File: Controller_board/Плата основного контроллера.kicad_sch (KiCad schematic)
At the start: 38 parts, among them J3 DebugUSART (PinHeader_01x03_P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, J4 Debug GPIO (PinHeader_01x02_P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, Q1 DTC114ECA (SOT-23), Q2 DTC114ECA (SOT-23), U1 ADM3485EARZ-REEL (SOIC-8), U2 ADUM1401CRWZ-RL, SO16W, U5 SMU02N-05

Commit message: Change ISOLATOR 03.06.24
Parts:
- removed U2: ADUM1401CRWZ-RL, SO16W, Package_SO:SOIC-16W_7.5x10.3mm_P1.27mm, symbol Isolator:ADuM1401xRW
- added U2: π141M3x, Package_SO:SOIC-16_3.9x9.9mm_P1.27mm, symbol Isolator:π141M3x
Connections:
- net +3.3VRS485: now also U2.16 (VDD2)
- net +5V: now also U2.1 (VDD1)
- net GND1: now also U2.15 (GND2), U2.9 (GND2)
- net GNDD: now also U2.2 (GND1), U2.8 (GND1)
- net USART2_RTS: now also U2.5 (VIC)
- net USART2_RX: now also U2.6 (VOD)
- net USART2_TX: now also U2.4 (VIB)
- net at R1.1, U1.1 (RO): now also U2.11 (VID)
- net at R2.1: now also U2.10 (VE2)
- net at R7.2, U1.2 (~{RE}), U1.3 (DE): now also U2.12 (VOC)
- net at U1.4 (DI): now also U2.13 (VOB)
- net at R5.2: now also U2.7 (VE1)
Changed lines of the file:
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@@
-    )
-  )
-  (symbol (lib_id "Isolator:ADuM1401xRW") (at 138.43 43.18 180) (unit 1)
-    (in_bom yes) (on_board yes) (dnp no)
-    (property "Reference" "U2" (at 138.43 25.4 0)
-      (effects (font (size 1.27 1.27)))
-    )
-    (property "Value" "ADUM1401CRWZ-RL, SO16W" (at 138.43 27.94 0)
-      (effects (font (size 1.27 1.27)))
-    )
-    (property "Footprint" "Package_SO:SOIC-16W_7.5x10.3mm_P1.27mm" (at 138.43 28.575 0)
-      (effects (font (size 1.27 1.27)) hide)
-    )
-    (property "Datasheet" "https://www.analog.com/media/en/technical-documentation/data-sheets/ADUM1400_1401_1402.pdf" (at 158.75 43.18 0)
-      (effects (font (size 1.27 1.27)) hide)
-    )
-    (pin "10")
-    (pin "9")
-    (pin "4")
-    (pin "8")
-    (pin "1")
-    (pin "13")
-    (pin "2")
-    (pin "11")
-    (pin "7")
-    (pin "5")
-    (pin "12")
-    (pin "3")
-    (pin "6")
-    (pin "14")
-    (pin "16")
-    (pin "15")
-    (instances
-      (project "Плата основного контроллера"
-        (path "/0ad4c27f-47f6-4faf-ae8a-ed32884f7b20"
-          (reference "U2") (unit 1)
-        )
-      )
-      (project "Плата внешних шаговых двигателей"
-        (path "/7f8f7dc9-8c50-44ed-985c-35a6d8c67be0/0d239b34-7914-40bc-9b83-7e562c30defe"
-          (reference "U4") (unit 1)
-        )
-        (path "/7f8f7dc9-8c50-44ed-985c-35a6d8c67be0"
-          (reference "U2") (unit 1)
-        )
-      )
     )
   )
@@
         )
       )
+    )
+  )
+  (symbol (lib_id "Isolator:π141M3x") (at 138.43 43.18 180) (unit 1)
+    (in_bom yes) (on_board yes) (dnp no) (fields_autoplaced)
+    (property "Reference" "U2" (at 138.43 25.4 0)
+      (effects (font (size 1.27 1.27)))
+    )
+    (property "Value" "π141M3x" (at 138.43 27.94 0)
+      (effects (font (size 1.27 1.27)))
+    )
+    (property "Footprint" "Package_SO:SOIC-16_3.9x9.9mm_P1.27mm" (at 138.43 28.575 0)
+      (effects (font (size 1.27 1.27)) hide)
+    )
+    (property "Datasheet" "https://wmsc.lcsc.com/wmsc/upload/file/pdf/v2/lcsc/2001082007_2Pai-Semi--141M30_C471604.pdf" (at 158.75 43.18 0)
+      (effects (font (size 1.27 1.27)) hide)
+    )
+    (pin "6")
+    (pin "16")
+    (pin "11")
+    (pin "13")
+    (pin "10")
+    (pin "12")
+    (pin "3")
+    (pin "14")
+    (pin "4")
+    (pin "8")
+    (pin "5")
+    (pin "2")
+    (pin "9")
+    (pin "7")
+    (pin "15")
+    (pin "1")
+    (instances
+      (project "Плата основного контроллера"
+        (path "/0ad4c27f-47f6-4faf-ae8a-ed32884f7b20"
+          (reference "U2") (unit 1)
+        )
+      )

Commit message: pcb and schems main controller 07.06.24
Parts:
- added TP1 (x9): TestPoint, PCM_4ms_TestPoint:TestPoint_D1, symbol Connector:TestPoint
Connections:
- net +5V: now also TP1.1
- net GND1: now also RS1.5 (Pin_5), RS1.6 (Pin_6), RS3.7 (Pin_7), RS3.8 (Pin_8)
- net UART6_DE: now also J3.1 (Pin_1); no longer J3.3 (Pin_3)
- net USART2_RTS: now also TP1.1
- net USART2_RX: now also TP1.1
- net USART2_TX: now also TP1.1
- net USART6_RX: now also J3.3 (Pin_3); no longer J3.2 (Pin_2)
- net USART6_TX: now also J3.2 (Pin_2); no longer J3.1 (Pin_1)
- net at R31.1, R6.2, RS1.4 (Pin_4)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: now also TP1.1
- net at R3.1, R31.2, RS1.3 (Pin_3)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: now also TP1.1
- net at R1.1, U1.1 (RO), U2.11 (VID): now also TP1.1
- net at R7.2, U1.2 (~{RE}), U1.3 (DE)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: now also TP1.1
- net at U1.4 (DI), U2.13 (VOB): now also TP1.1
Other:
- sheet RTS_ISO ports: added +3.3V; removed none
- moved on the sheet: R5

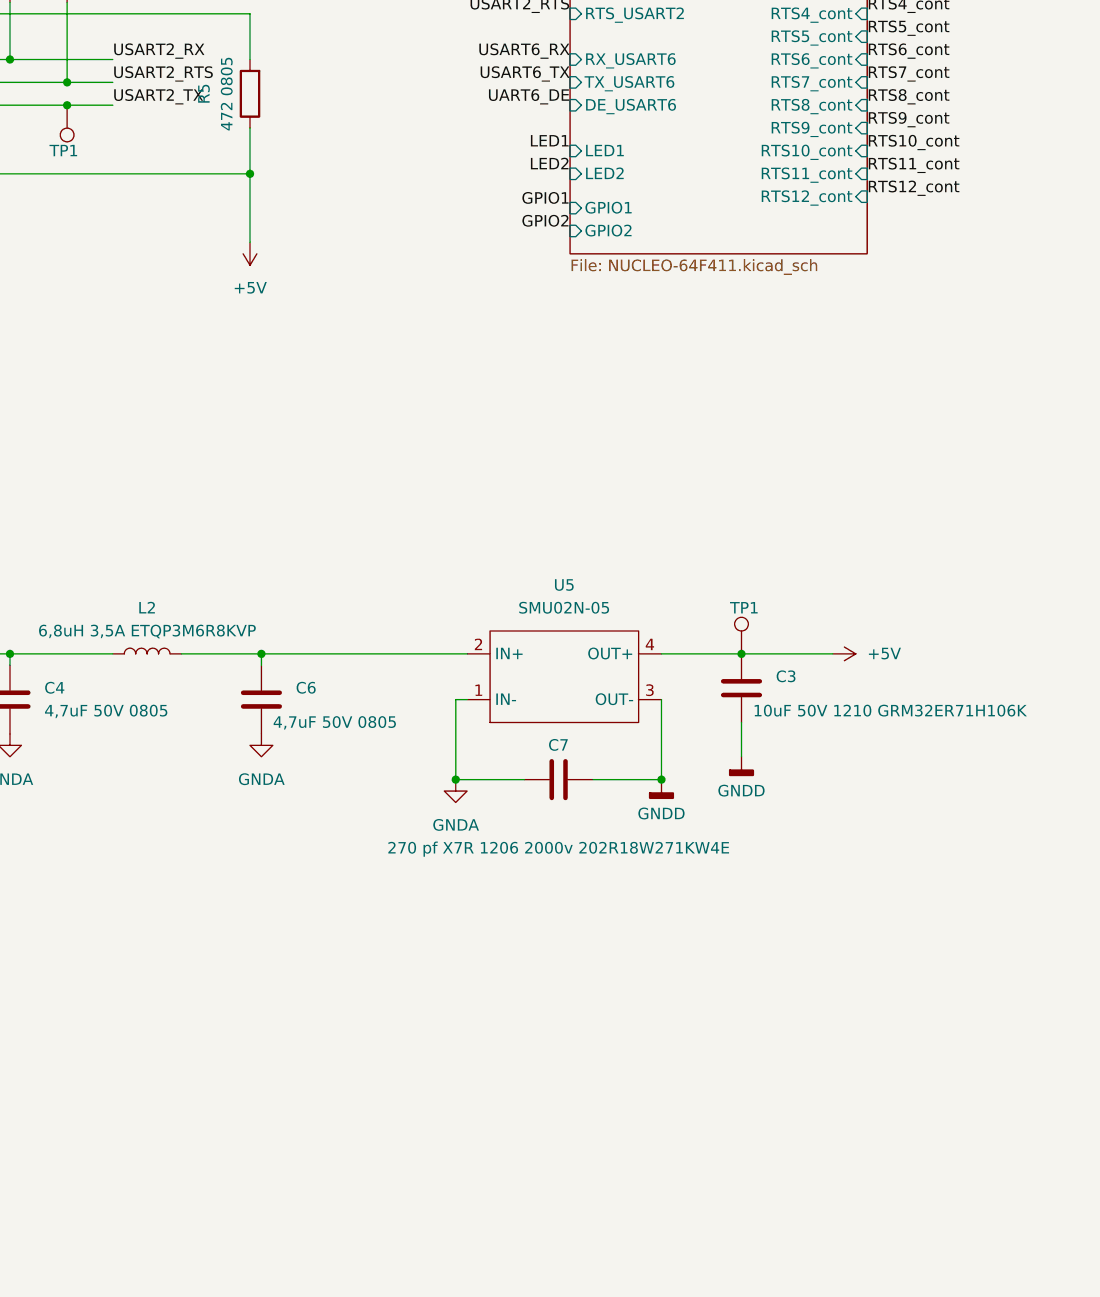
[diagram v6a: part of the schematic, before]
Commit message: Main controller +3.3V RS485 schems and PCB
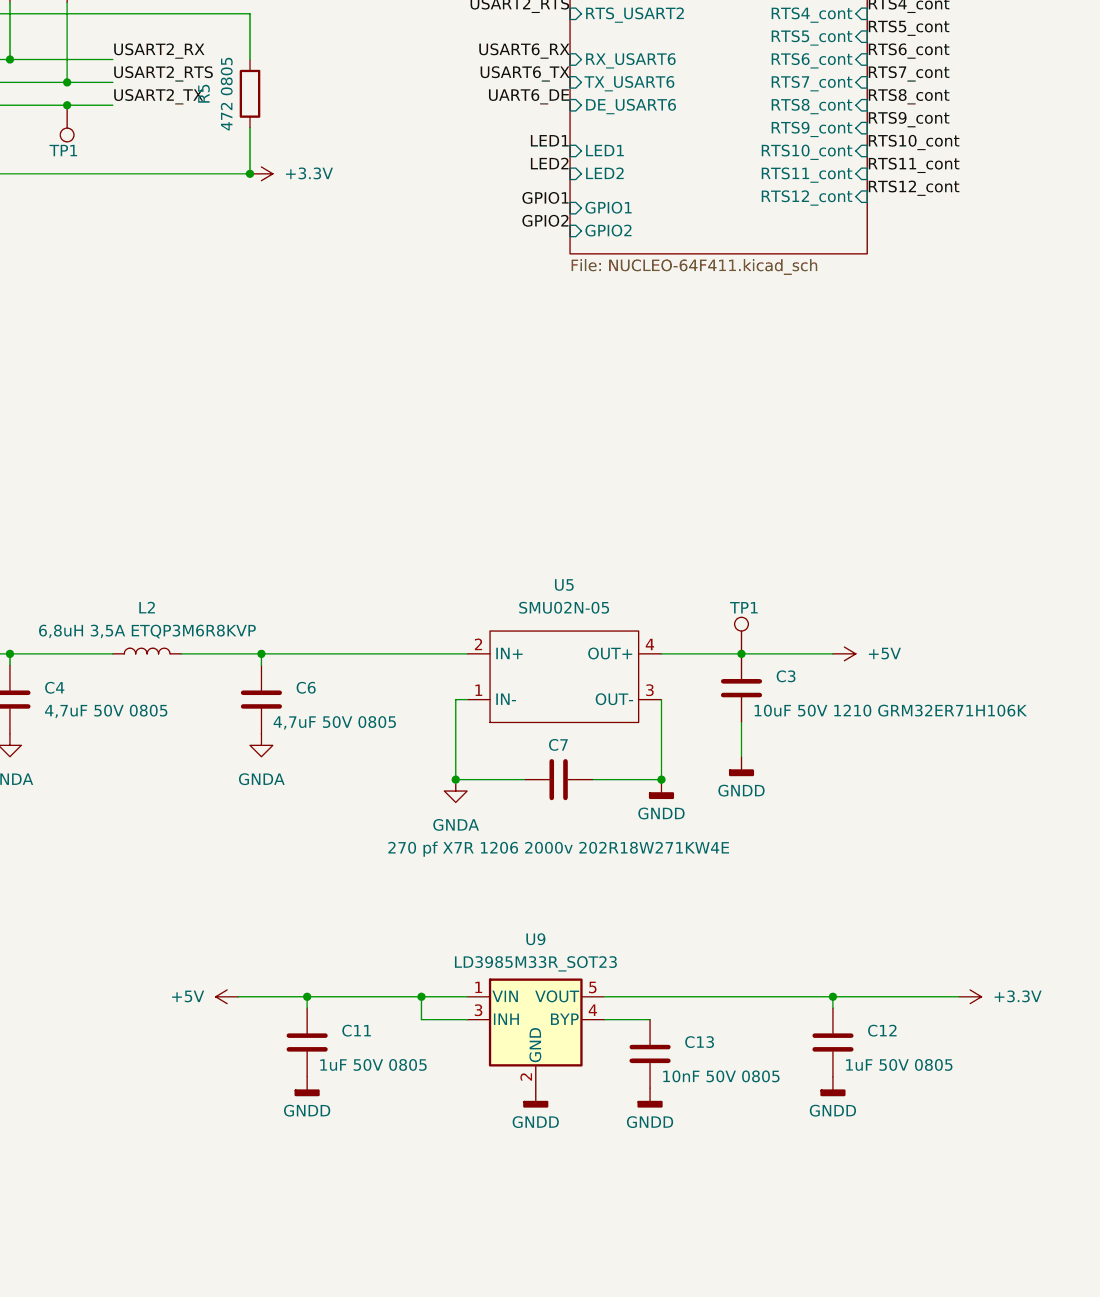
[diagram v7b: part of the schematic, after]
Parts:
- added C11, C12: 1uF 50V 0805, PCM_Capacitor_SMD_AKL:C_0805_2012Metric_Pad1.18x1.45mm_HandSolder, symbol Device:C
- added C13: 10nF 50V 0805, PCM_Capacitor_SMD_AKL:C_0805_2012Metric_Pad1.18x1.45mm_HandSolder, symbol Device:C
- added U9: LD3985M33R_SOT23, Package_TO_SOT_SMD:SOT-23-5, symbol Regulator_Linear:LD3985M33R_SOT23
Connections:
- net +5V: now also C11.1, U9.1 (VIN), U9.3 (INH); no longer C9.2, R5.1, U2.1 (VDD1)
- net GNDD: now also C11.2, C12.2, C13.2, U9.2 (GND)
- new net: C13.1, U9.4 (BYP)
- new net +3V3: C12.1, C9.2, R5.1, U2.1 (VDD1), U9.5 (VOUT)

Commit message: Main controller renew schems and PCB
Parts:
- removed U9: LD3985M33R_SOT23, Package_TO_SOT_SMD:SOT-23-5, symbol Regulator_Linear:LD3985M33R_SOT23
- added IC1: LD1117-3.3V-SOT223, PCM_Package_TO_SOT_SMD_AKL:SOT-89-3_BigPads, symbol PCM_4ms_Regulator:LD1117-3.3V-SOT223
- C1: value 1uF 100V 0805 -> 1uF 50V 0805
- C12: value 1uF 50V 0805 -> 10uF 16V 0805
- C13: value 10nF 50V 0805 -> 0,1uF 50V 0805
- C5, C8, C9: value 0,1uF 100V 0805 -> 0,1uF 50V 0805
- U2: value π141M3x -> π141M30 (SOIC-16)
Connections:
- net +3V3: now also IC1.2 (OUT)
- net +5V: now also C13.1, IC1.3 (IN)
- net GNDD: now also IC1.1 (ADJ)
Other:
- moved on the sheet: C11, C12
